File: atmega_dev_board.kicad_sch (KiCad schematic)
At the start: 39 parts, among them J1 1x15 Pin Header, J2 U263-163N-4BLS1735, J3 1x15 Pin Header, J4 2x3 Pin Header, SW1 Push Button, SW2 Push Button, U1 78L05G-AB3-R, U2 HT7533-1, U3 ATmega328P-A, U4 CP2102N-Axx-xQFN28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

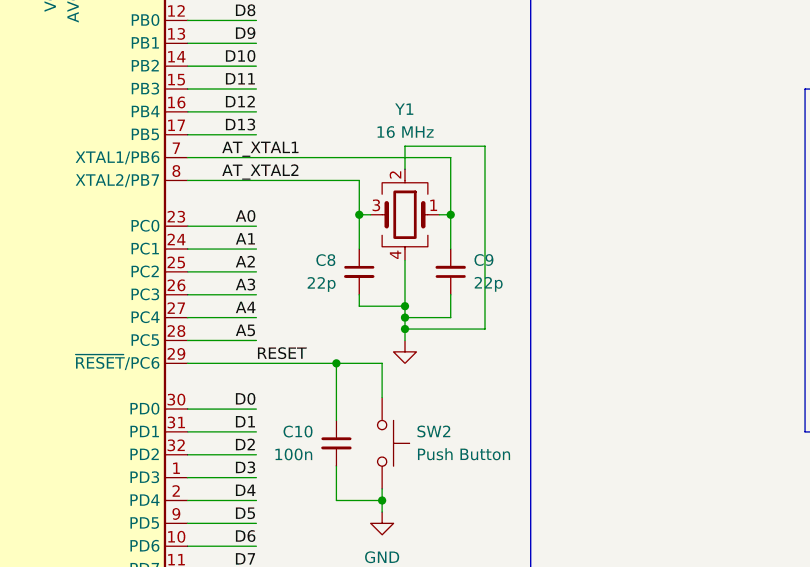
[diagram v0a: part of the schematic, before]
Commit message: Update loading cap values (from 22p to 12p)
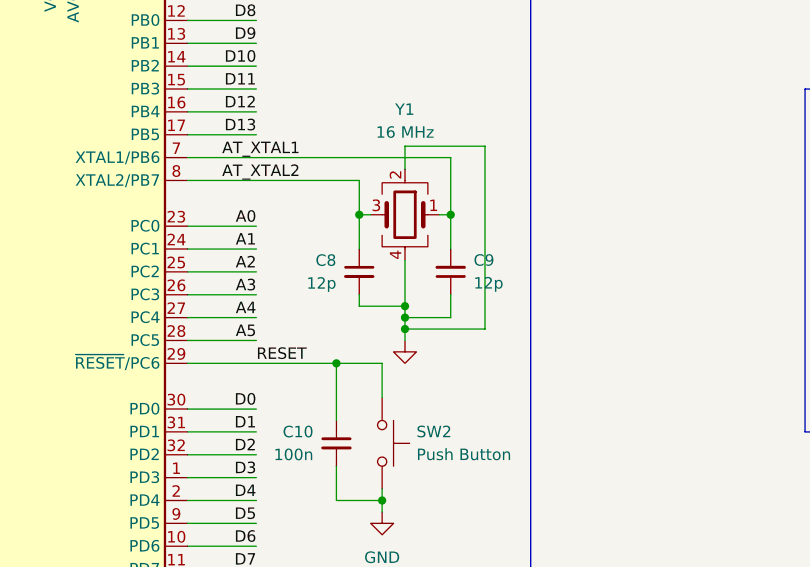
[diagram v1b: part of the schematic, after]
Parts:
- C8, C9: value 22p -> 12p; JLCPCB Part# C2991405 -> C38523
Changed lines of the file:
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@@
 			)
 		)
-		(property "Value" "22p"
+		(property "Value" "12p"
 			(at 171.45 116.8462 0)
 			(effects
@@
 			)
 		)
-		(property "Datasheet" "https://wmsc.lcsc.com/wmsc/upload/file/pdf/v2/lcsc/2204131745_Walsin-Tech-Corp-0603N220J100CT-C_C2991405.pdf"
+		(property "Datasheet" "https://wmsc.lcsc.com/wmsc/upload/file/pdf/v2/lcsc/2304140030_Samsung-Electro-Mechanics-CL10C120JB8NNNC_C38523.pdf"
 			(at 173.99 115.57 0)
 			(effects
@@
 			)
 		)
-		(property "JLCPCB Part#" "C2991405"
+		(property "JLCPCB Part#" "C38523"
 			(at 173.99 115.57 0)
 			(effects
@@
 			)
 		)
-		(property "Value" "22p"
+		(property "Value" "12p"
 			(at 186.69 116.8335 0)
 			(effects
@@
 			)
 		)
-		(property "Datasheet" "https://wmsc.lcsc.com/wmsc/upload/file/pdf/v2/lcsc/2204131745_Walsin-Tech-Corp-0603N220J100CT-C_C2991405.pdf"
+		(property "Datasheet" "https://wmsc.lcsc.com/wmsc/upload/file/pdf/v2/lcsc/2304140030_Samsung-Electro-Mechanics-CL10C120JB8NNNC_C38523.pdf"
 			(at 184.15 115.57 0)
 			(effects
@@
 			)
 		)
-		(property "JLCPCB Part#" "C2991405"
+		(property "JLCPCB Part#" "C38523"
 			(at 184.15 115.57 0)
 			(effects

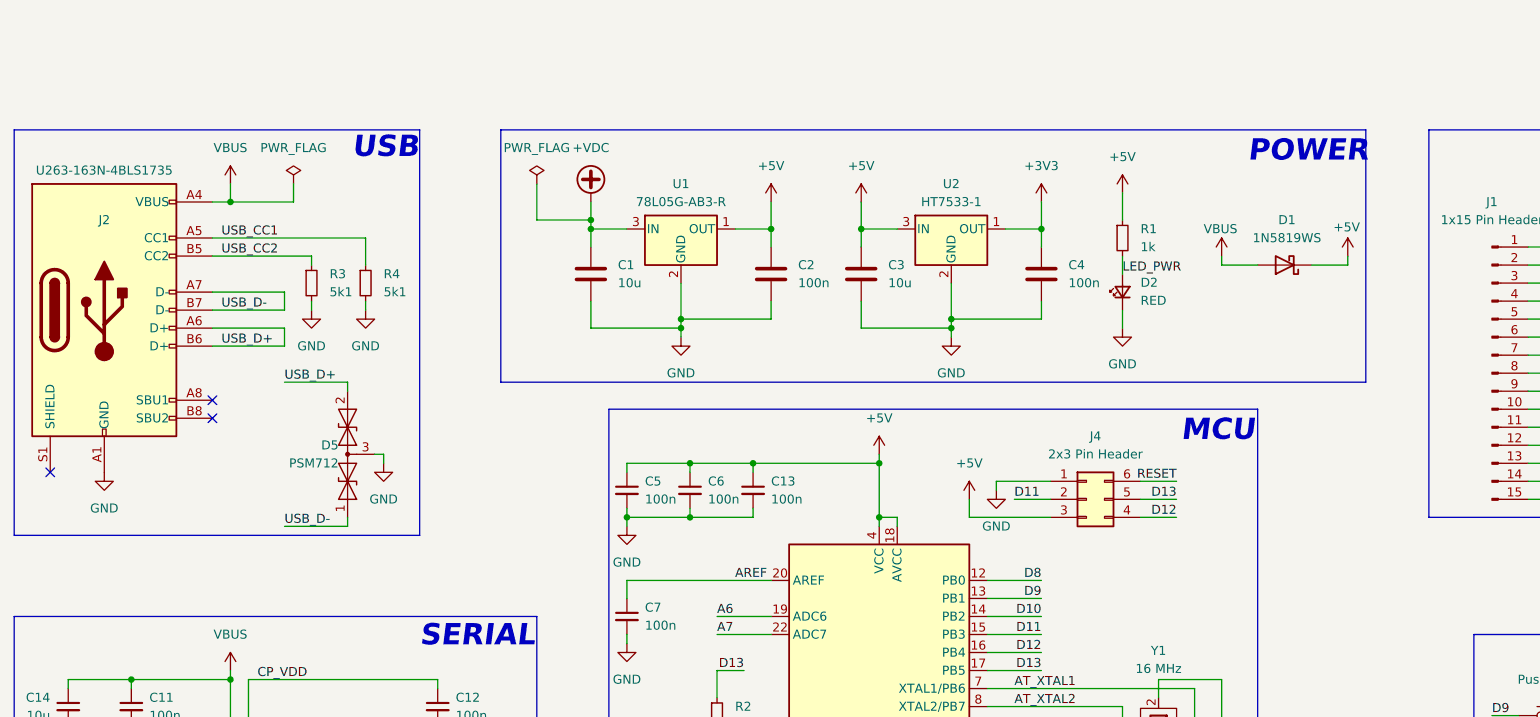
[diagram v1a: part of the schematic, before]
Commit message: Swap out TVS diodes. Ground USB shield
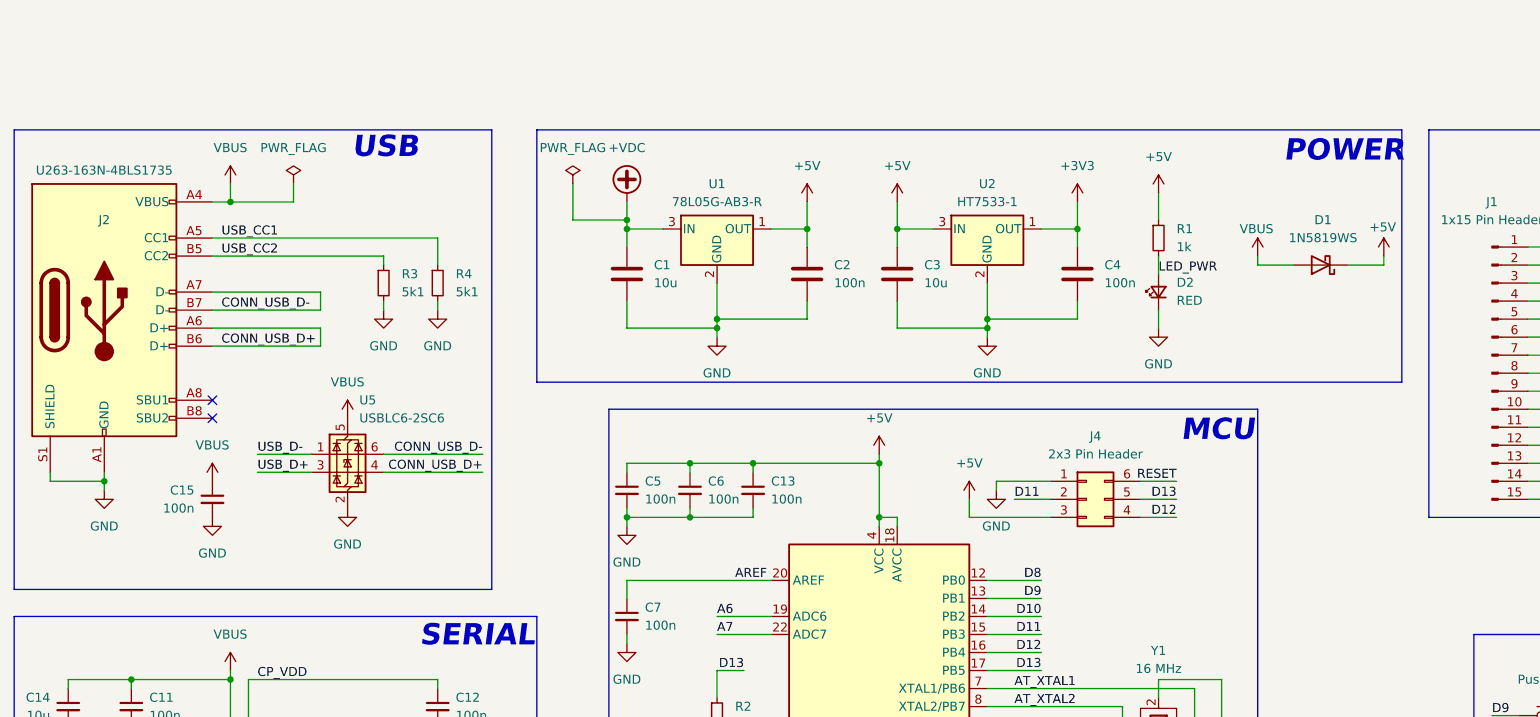
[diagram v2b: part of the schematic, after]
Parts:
- removed D5: PSM712, Package_TO_SOT_SMD:SOT-23, symbol Diode:SM712_SOT23
- added C15: 100n, Capacitor_SMD:C_0603_1608Metric, symbol Device:C_Small
- added U5: USBLC6-2SC6, Package_TO_SOT_SMD:SOT-23-6, symbol Power_Protection:USBLC6-2SC6
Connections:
- net GND: now also J2.S1 (SHIELD), C15.2, U5.2 (GND)
- net USB_D+: now also U5.3 (I/O2); no longer J2.A6 (D+), J2.B6 (D+)
- net USB_D-: now also U5.1 (I/O1); no longer J2.A7 (D-), J2.B7 (D-)
- net VBUS: now also C15.1, U5.5 (VBUS)
- new net CONN_USB_D+: J2.A6 (D+), J2.B6 (D+), U5.4 (I/O2)
- new net CONN_USB_D-: J2.A7 (D-), J2.B7 (D-), U5.6 (I/O1)
- no-connect marks 20 -> 19
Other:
- moved on the sheet: C1, C2, C3, C4, D1, D2, R1, R3, R4, U1, U2

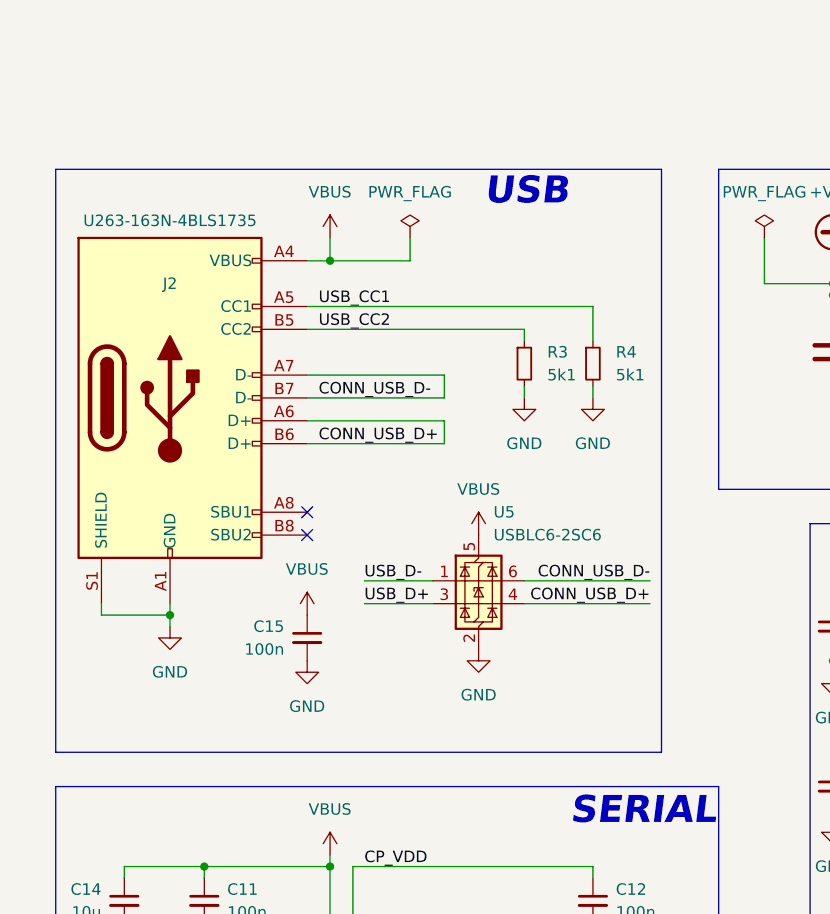
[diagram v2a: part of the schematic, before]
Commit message: Update BOM and component values
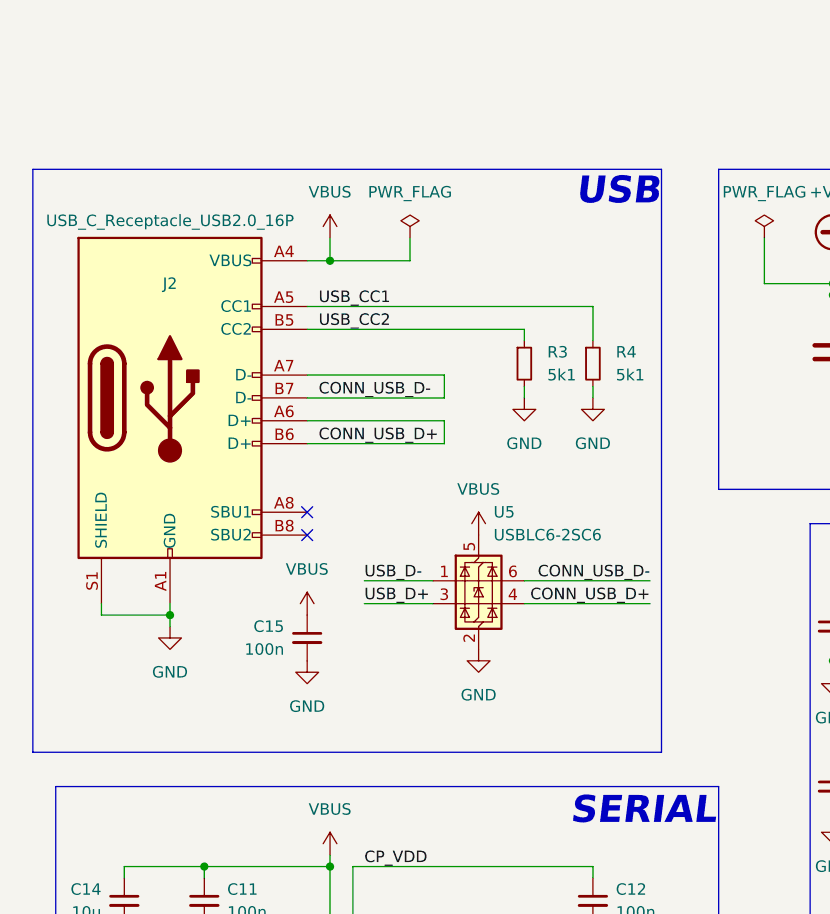
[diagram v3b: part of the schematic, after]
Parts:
- C1, C14, C3: Manufacturer Part# (none) -> CL10A106KP8NNNC
- C10, C11, C12, C13, C15, C2, C4, C5, C6, C7: Manufacturer Part# (none) -> CC0603KRX7R9BB104
- C8, C9: Manufacturer Part# (none) -> CL10C120JB8NNNC
- D1: Manufacturer Part# (none) -> 1N5819WS
- D2, D4, D6, D7: Manufacturer Part# (none) -> KT-0603R
- D3: Manufacturer Part# (none) -> XL-5050RGBC-WS2812B
- J2: value U263-163N-4BLS1735 -> USB_C_Receptacle_USB2.0_16P; JLCPCB Part# C2931474 -> C7527694; Manufacturer Part# (none) -> XUBF-0336-0817B
- R1, R2, R5, R6: Manufacturer Part# (none) -> 0603WAF1001T5E
- R3, R4: Manufacturer Part# (none) -> 0603WAF5101T5E
- SW1, SW2: Manufacturer Part# (none) -> TS-1187A-B-A-B
- U1: Manufacturer Part# (none) -> 78L05G-AB3-R
- U2: Manufacturer Part# (none) -> HT7533-1
- U3: Manufacturer Part# (none) -> ATMEGA328P-AU
- U4: Manufacturer Part# (none) -> CP2102-GMR
- Y1: Manufacturer Part# (none) -> X322516MLB4SI

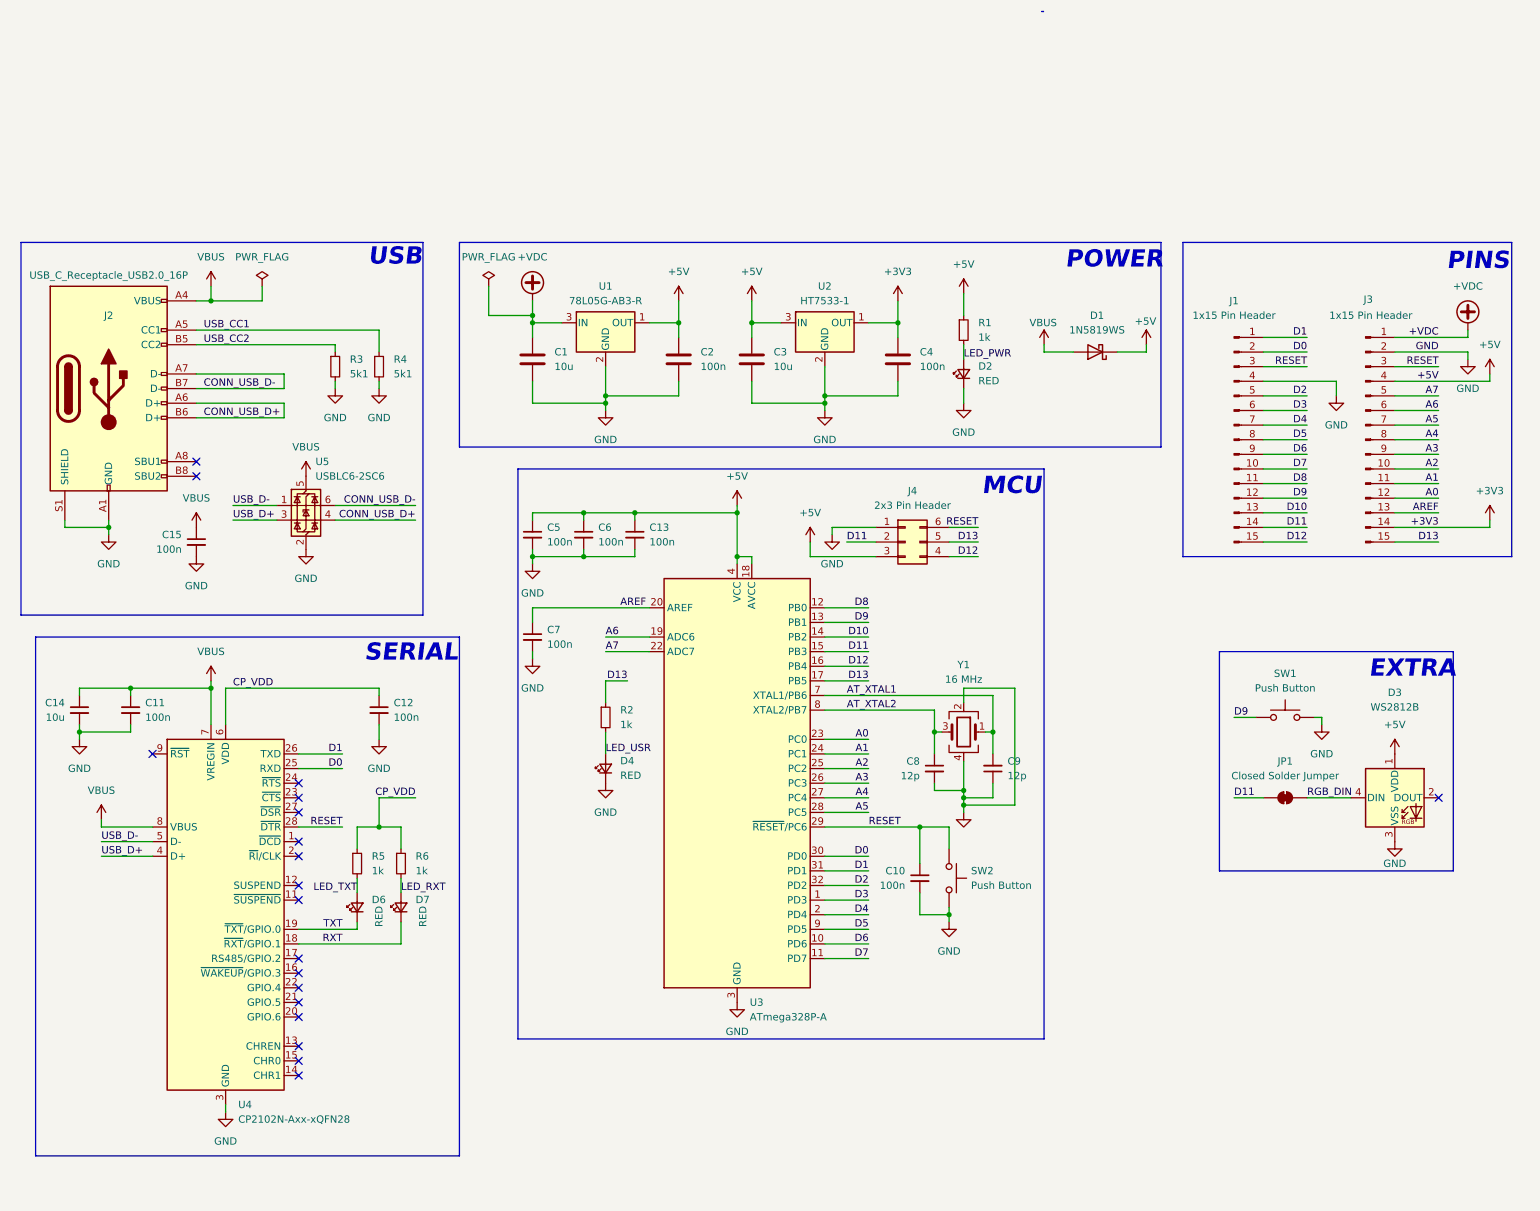
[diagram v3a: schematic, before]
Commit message: lots
Sch: Add feducials
PCB: Add pin labels to silkscreen
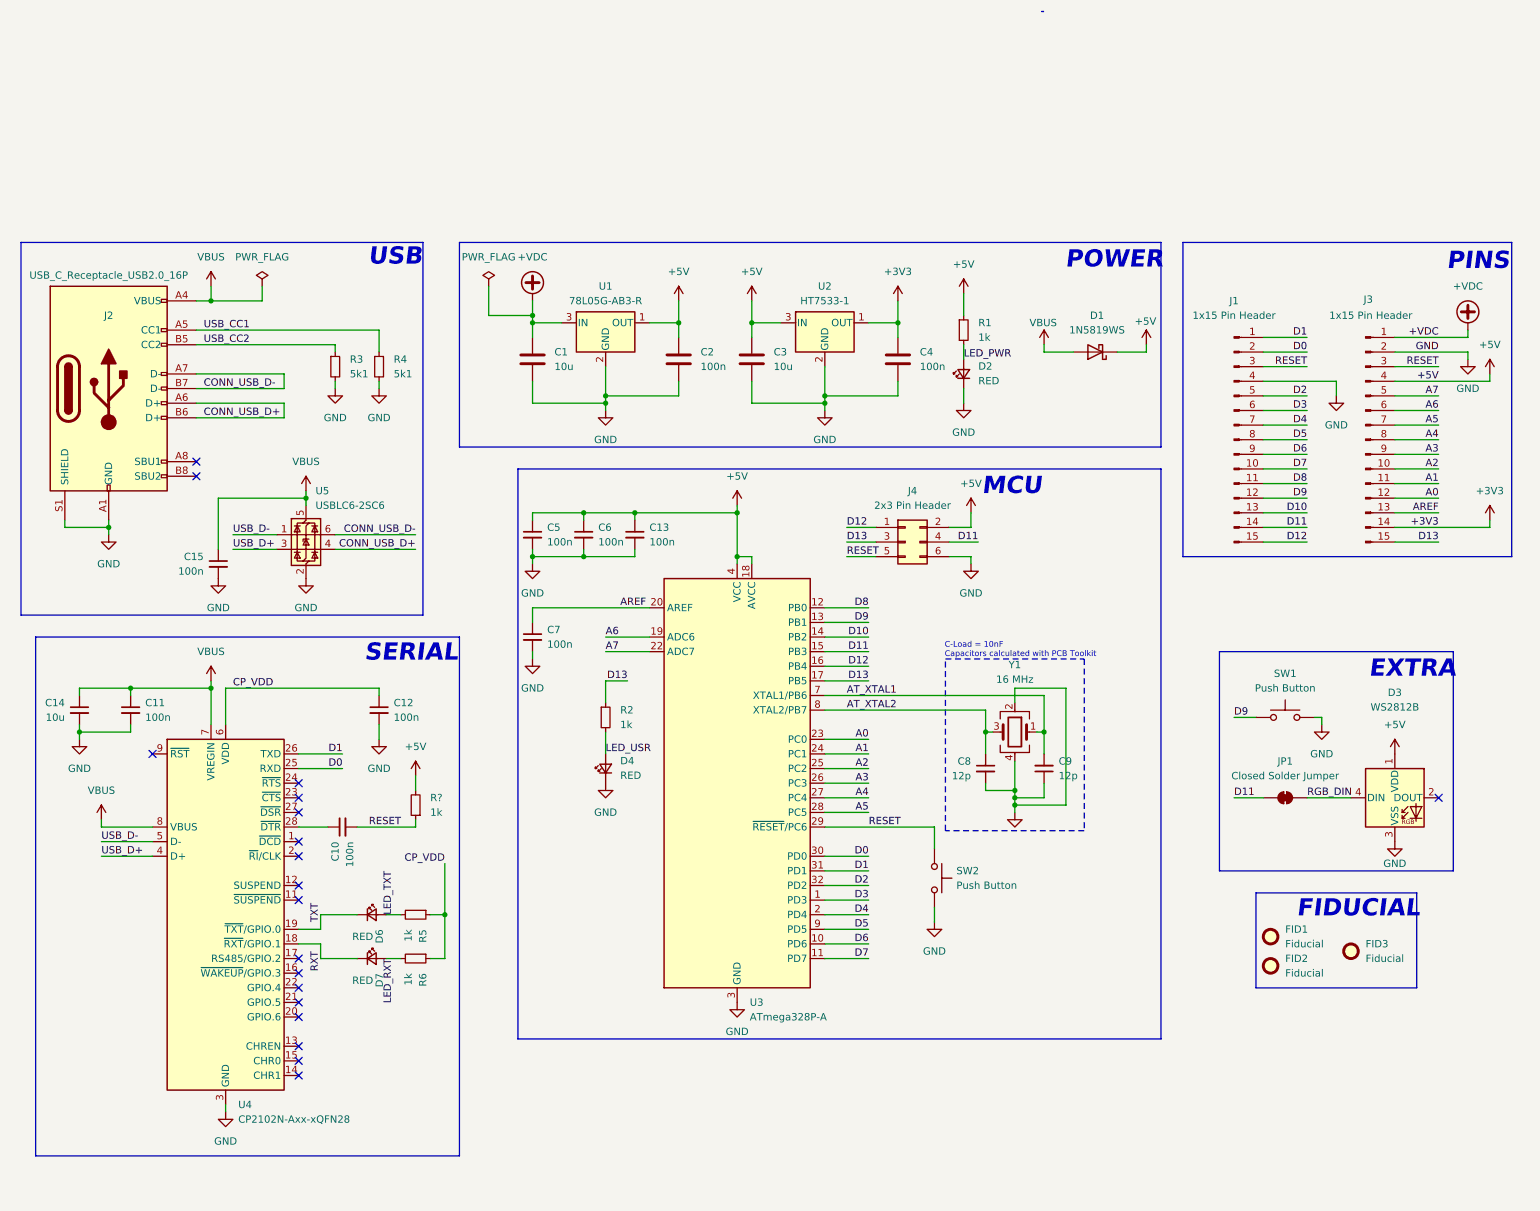
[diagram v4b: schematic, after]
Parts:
- added FID1, FID2, FID3: Fiducial, Fiducial:Fiducial_0.5mm_Mask1mm, symbol Mechanical:Fiducial
- added R?: 1k, Resistor_SMD:R_0603_1608Metric, symbol Device:R_Small
- J4: symbol Connector_Generic:Conn_02x03_Counter_Clockwise -> Connector_Generic:Conn_02x03_Odd_Even
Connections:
- net +5V: now also J4.2 (Pin_2), R?.2; no longer J4.3 (Pin_3)
- net D11: now also J4.4 (Pin_4); no longer J4.2 (Pin_2)
- net D12: now also J4.1 (Pin_1); no longer J4.4 (Pin_4)
- net D13: now also J4.3 (Pin_3); no longer J4.5 (Pin_5)
- net GND: now also J4.6 (Pin_6); no longer C10.2, J4.1 (Pin_1)
- net RESET: now also C10.2, J4.5 (Pin_5), R?.1; no longer C10.1, J4.6 (Pin_6), U4.28 (~{DTR})
- new net: C10.1, U4.28 (~{DTR})
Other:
- note added: "C-Load = 10nF Capacitors calculated with PCB Toolkit"
- note added: "FIDUCIAL"
- moved on the sheet: C10, C15, C8, C9, D6, D7, R5, R6, SW2, U5, Y1
